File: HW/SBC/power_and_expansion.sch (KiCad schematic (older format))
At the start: 9 parts, among them J4 POWER IN, J5 Expansion Port, U11 LM7805CT

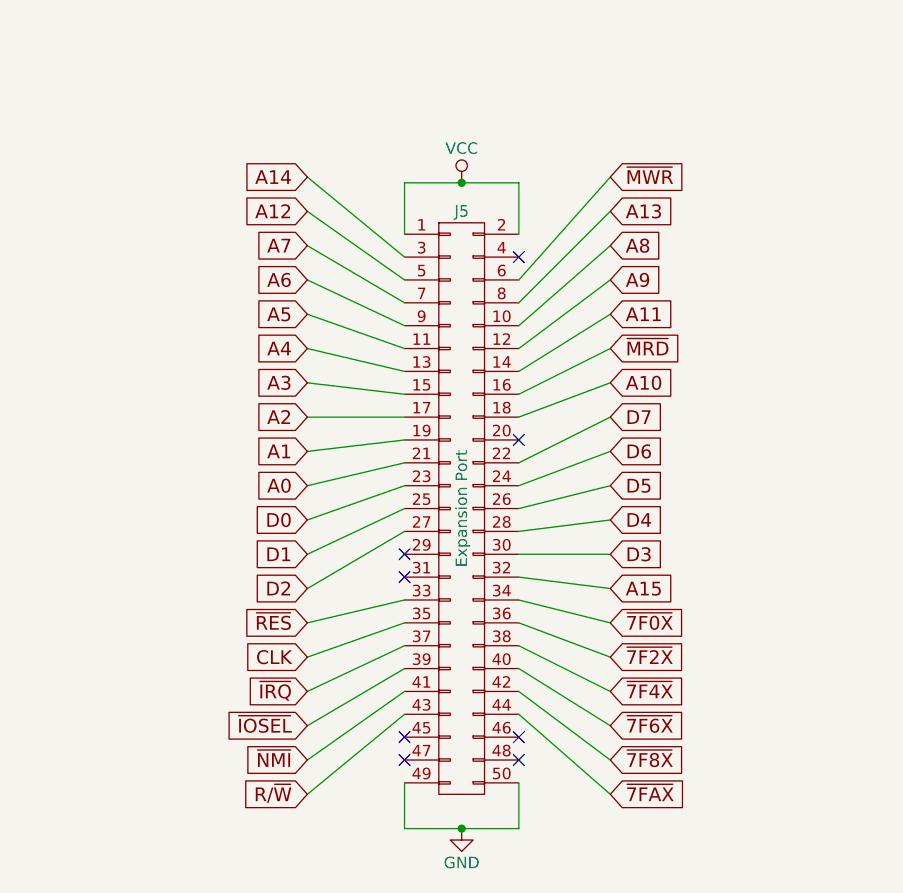
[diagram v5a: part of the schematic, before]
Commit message: New SBC PCB. Started to split pluto_kernel.asm into bios, monitor and miniassembler/disassembler. Various other updates.
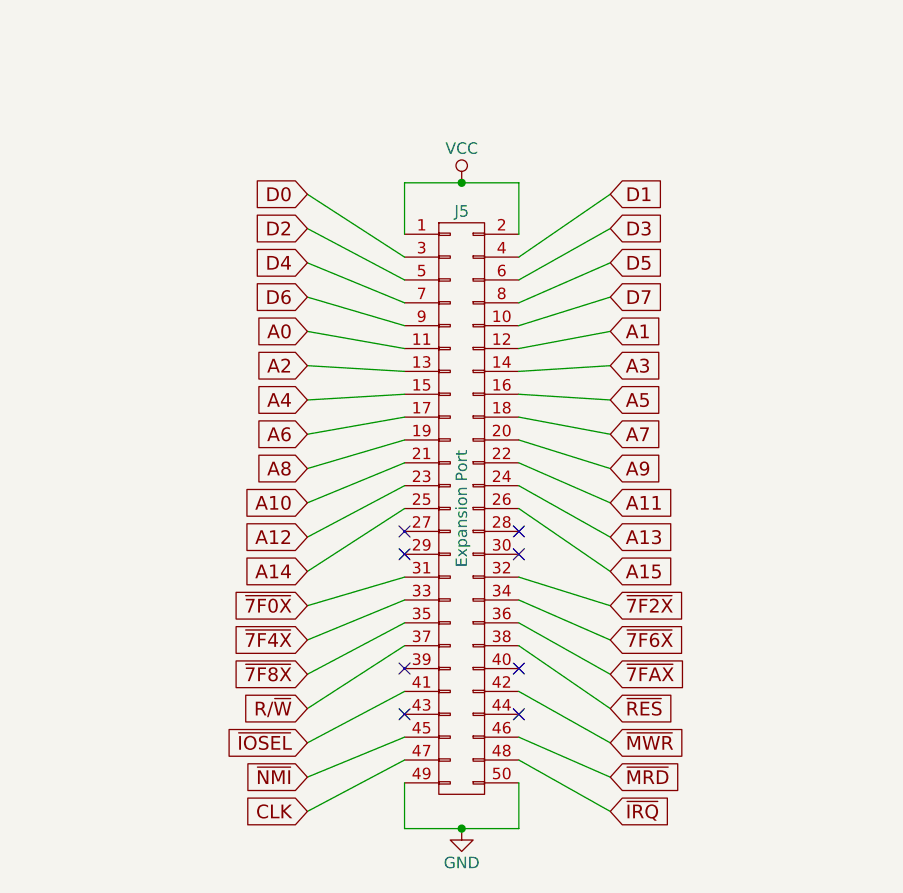
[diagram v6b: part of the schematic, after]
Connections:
- net A0: now also J5.11 (P11); no longer J5.21 (P21)
- net A1: now also J5.12 (P12); no longer J5.19 (P19)
- net A10: now also J5.21 (P21); no longer J5.18 (P18)
- net A11: now also J5.22 (P22); no longer J5.14 (P14)
- net A12: now also J5.23 (P23); no longer J5.5 (P5)
- net A13: now also J5.24 (P24); no longer J5.8 (P8)
- net A14: now also J5.25 (P25); no longer J5.3 (P3)
- net A15: now also J5.26 (P26); no longer J5.32 (P32)
- net A2: now also J5.13 (P13); no longer J5.17 (P17)
- net A3: now also J5.14 (P14); no longer J5.15 (P15)
- net A4: now also J5.15 (P15); no longer J5.13 (P13)
- net A5: now also J5.16 (P16); no longer J5.11 (P11)
- net A6: now also J5.17 (P17); no longer J5.9 (P9)
- net A7: now also J5.18 (P18); no longer J5.7 (P7)
- net A8: now also J5.19 (P19); no longer J5.10 (P10)
- net A9: now also J5.20 (P20); no longer J5.12 (P12)
- net CLK: now also J5.47 (P47); no longer J5.35 (P35)
- net D0: now also J5.3 (P3); no longer J5.23 (P23)
- net D1: now also J5.4 (P4); no longer J5.25 (P25)
- net D2: now also J5.5 (P5); no longer J5.27 (P27)
- net D3: now also J5.6 (P6); no longer J5.30 (P30)
- net D4: now also J5.7 (P7); no longer J5.28 (P28)
- net D5: now also J5.8 (P8); no longer J5.26 (P26)
- net D6: now also J5.9 (P9); no longer J5.24 (P24)
- net D7: now also J5.10 (P10); no longer J5.22 (P22)
- net R/~W: now also J5.37 (P37); no longer J5.43 (P43)
- net ~7F0X: now also J5.31 (P31); no longer J5.34 (P34)
- net ~7F2X: now also J5.32 (P32); no longer J5.36 (P36)
- net ~7F4X: now also J5.33 (P33); no longer J5.38 (P38)
- net ~7F6X: now also J5.34 (P34); no longer J5.40 (P40)
- net ~7F8X: now also J5.35 (P35); no longer J5.42 (P42)
- net ~7FAX: now also J5.36 (P36); no longer J5.44 (P44)
- net ~IOSEL: now also J5.41 (P41); no longer J5.39 (P39)
- net ~IRQ: now also J5.48 (P48); no longer J5.37 (P37)
- net ~MRD: now also J5.46 (P46); no longer J5.16 (P16)
- net ~MWR: now also J5.42 (P42); no longer J5.6 (P6)
- net ~NMI: now also J5.45 (P45); no longer J5.41 (P41)
- net ~RES: now also J5.38 (P38); no longer J5.33 (P33)
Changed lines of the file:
@@
 $EndComp
 $Comp
-L VCC #PWR025
+L VCC #PWR024
 U 1 1 58D5EE10
 P 5625 1650
-F 0 "#PWR025" H 5625 1500 50  0001 C CNN
+F 0 "#PWR024" H 5625 1500 50  0001 C CNN
 F 1 "VCC" H 5625 1800 50  0000 C CNN
 F 2 "" H 5625 1650 50  0001 C CNN
@@
 	3225 1650 5625 1650
 $Comp
-L VCC #PWR026
+L VCC #PWR025
 U 1 1 58D7686C
 P 3600 3500
-F 0 "#PWR026" H 3600 3350 50  0001 C CNN
+F 0 "#PWR025" H 3600 3350 50  0001 C CNN
 F 1 "VCC" H 3600 3650 50  0000 C CNN
 F 2 "" H 3600 3500 50  0001 C CNN
@@
 Connection ~ 3600 3500
 $Comp
-L GND #PWR027
+L GND #PWR026
 U 1 1 58D76B4A
 P 3600 6325
-F 0 "#PWR027" H 3600 6075 50  0001 C CNN
+F 0 "#PWR026" H 3600 6075 50  0001 C CNN
 F 1 "GND" H 3600 6175 50  0000 C CNN
 F 2 "" H 3600 6325 50  0001 C CNN
@@
 	3850 6325 3850 6125
 Connection ~ 3600 6325
-NoConn ~ 3850 3825
-Text GLabel 2925 4825 0    60   Input ~ 0
+Text GLabel 2925 4150 0    60   Input ~ 0
 A0
-Text GLabel 2925 4675 0    60   Input ~ 0
+Text GLabel 4250 4150 2    60   Input ~ 0
 A1
-Text GLabel 2925 4525 0    60   Input ~ 0
+Text GLabel 2925 4300 0    60   Input ~ 0
 A2
-Text GLabel 2925 4375 0    60   Input ~ 0
+Text GLabel 4250 4300 2    60   Input ~ 0
 A3
-Text GLabel 2925 4225 0    60   Input ~ 0
+Text GLabel 2925 4450 0    60   Input ~ 0
 A4
-Text GLabel 2925 4075 0    60   Input ~ 0
+Text GLabel 4250 4450 2    60   Input ~ 0
 A5
-Text GLabel 2925 3925 0    60   Input ~ 0
+Text GLabel 2925 4600 0    60   Input ~ 0
 A6
-Text GLabel 2925 3775 0    60   Input ~ 0
+Text GLabel 4250 4600 2    60   Input ~ 0
 A7
-Text GLabel 4250 3775 2    60   Input ~ 0
+Text GLabel 2925 4750 0    60   Input ~ 0
 A8
-Text GLabel 4250 3925 2    60   Input ~ 0
+Text GLabel 4250 4750 2    60   Input ~ 0
 A9
-Text GLabel 4250 4375 2    60   Input ~ 0
+Text GLabel 2925 4900 0    60   Input ~ 0
 A10
-Text GLabel 4250 4075 2    60   Input ~ 0
+Text GLabel 4250 4900 2    60   Input ~ 0
 A11
-Text GLabel 2925 3625 0    60   Input ~ 0
+Text GLabel 2925 5050 0    60   Input ~ 0
 A12
-Text GLabel 4250 3625 2    60   Input ~ 0
+Text GLabel 4250 5050 2    60   Input ~ 0
 A13
-Text GLabel 2925 3475 0    60   Input ~ 0
+Text GLabel 2925 5200 0    60   Input ~ 0
 A14
-Text GLabel 4250 5275 2    60   Input ~ 0
+Text GLabel 4250 5200 2    60   Input ~ 0
 A15
-Text GLabel 4250 3475 2    60   Input ~ 0
+Text GLabel 4250 5950 2    60   Input ~ 0
 ~MWR
-Text GLabel 4250 4225 2    60   Input ~ 0
+Text GLabel 4250 6100 2    60   Input ~ 0
 ~MRD
-Text GLabel 4250 5425 2    60   Input ~ 0
+Text GLabel 2925 5350 0    60   Input ~ 0
 ~7F0X
-Text GLabel 4250 5575 2    60   Input ~ 0
+Text GLabel 4250 5350 2    60   Input ~ 0
 ~7F2X
-Text GLabel 4250 5725 2    60   Input ~ 0
+Text GLabel 2925 5500 0    60   Input ~ 0
 ~7F4X
-Text GLabel 4250 5875 2    60   Input ~ 0
+Text GLabel 4250 5500 2    60   Input ~ 0
 ~7F6X
-Text GLabel 4250 6025 2    60   Input ~ 0
+Text GLabel 2925 5650 0    60   Input ~ 0
 ~7F8X
-Text GLabel 2925 4975 0    60   Input ~ 0
+Text GLabel 2925 3550 0    60   Input ~ 0
 D0
-Text GLabel 2925 5125 0    60   Input ~ 0
+Text GLabel 4250 3550 2    60   Input ~ 0
 D1
-Text GLabel 2925 5275 0    60   Input ~ 0
+Text GLabel 2925 3700 0    60   Input ~ 0
 D2
-Text GLabel 4250 5125 2    60   Input ~ 0
+Text GLabel 4250 3700 2    60   Input ~ 0
 D3
-Text GLabel 4250 4975 2    60   Input ~ 0
+Text GLabel 2925 3850 0    60   Input ~ 0
 D4
-Text GLabel 4250 4825 2    60   Input ~ 0
+Text GLabel 4250 3850 2    60   Input ~ 0
 D5
-Text GLabel 4250 4675 2    60   Input ~ 0
+Text GLabel 2925 4000 0    60   Input ~ 0
 D6
-Text GLabel 4250 4525 2    60   Input ~ 0
+Text GLabel 4250 4000 2    60   Input ~ 0
 D7
-Text GLabel 2925 5575 0    60   Input ~ 0
+Text GLabel 2925 6250 0    60   Input ~ 0
 CLK
-Text GLabel 2925 5725 0    60   Input ~ 0
+Text GLabel 4250 6250 2    60   Input ~ 0
 ~IRQ
-Text GLabel 2925 5875 0    60   Input ~ 0
+Text GLabel 2925 5950 0    60   Input ~ 0
 ~IOSEL
-Text GLabel 2925 6025 0    60   Input ~ 0
+Text GLabel 2925 6100 0    60   Input ~ 0
 ~NMI
-Text GLabel 2925 6175 0    60   Input ~ 0
+Text GLabel 2925 5800 0    60   Input ~ 0
 R/~W
-Text GLabel 2925 5425 0    60   Input ~ 0
+Text GLabel 4250 5800 2    60   Input ~ 0
 ~RES
-NoConn ~ 3350 5125
-NoConn ~ 3350 5225
-NoConn ~ 3850 4625
-NoConn ~ 3350 5925
-NoConn ~ 3350 6025
-Wire Wire Line
-	3350 3825 2925 3475
-Wire Wire Line
-	3350 3925 2925 3625
-Wire Wire Line
-	3350 4025 2925 3775
-Wire Wire Line
-	3350 4125 2925 3925
-Wire Wire Line
-	3350 4225 2925 4075
-Wire Wire Line
-	3350 4325 2925 4225
-Wire Wire Line
-	3350 4425 2925 4375
-Wire Wire Line
-	3350 4525 2925 4525
-Wire Wire Line
-	3350 4625 2925 4675
-Wire Wire Line
-	3350 4725 2925 4825
-Wire Wire Line
-	3350 4825 2925 4975
-Wire Wire Line
-	3350 4925 2925 5125
-Wire Wire Line
-	3350 5025 2925 5275
-Wire Wire Line
-	2925 5425 3350 5325
-Wire Wire Line
-	2925 5575 3350 5425
-Wire Wire Line
-	2925 5725 3350 5525
-Wire Wire Line
-	2925 5875 3350 5625
-Wire Wire Line
-	2925 6025 3350 5725
-Wire Wire Line
-	2925 6175 3350 5825
-Wire Wire Line
-	4250 3475 3850 3925
-Wire Wire Line
-	4250 3625 3850 4025
-Wire Wire Line
-	4250 3775 3850 4125
-Wire Wire Line
-	4250 3925 3850 4225
-Wire Wire Line
-	4250 4075 3850 4325
-Wire Wire Line
-	4250 4225 3850 4425
-Wire Wire Line
-	4250 4375 3850 4525
-Wire Wire Line
-	4250 4525 3850 4725
-Wire Wire Line
-	4250 4675 3850 4825
-Wire Wire Line
-	4250 4825 3850 4925
-Wire Wire Line
-	4250 4975 3850 5025
-Wire Wire Line
-	4250 5125 3850 5125
-Wire Wire Line
-	4250 5275 3850 5225
-Wire Wire Line
-	4250 5425 3850 5325
-Wire Wire Line
-	4250 5575 3850 5425
-Wire Wire Line
-	4250 5725 3850 5525
-Wire Wire Line
-	4250 5875 3850 5625
-Wire Wire Line
-	4250 6025 3850 5725
-NoConn ~ 3850 5925
-NoConn ~ 3850 6025
 Connection ~ 3225 2500
 $Comp
-L GND #PWR028
+L GND #PWR027
 U 1 1 58D85868
 P 5625 2500
-F 0 "#PWR028" H 5625 2250 50  0001 C CNN
+F 0 "#PWR027" H 5625 2250 50  0001 C CNN
 F 1 "GND" H 5625 2350 50  0000 C CNN
 F 2 "" H 5625 2500 50  0001 C CNN
@@
 	1    0    0    -1
 $EndComp
-Text GLabel 4250 6175 2    60   Input ~ 0
+Text GLabel 4250 5650 2    60   Input ~ 0
 ~7FAX
-Wire Wire Line
-	4250 6175 3850 5825
 $Comp
 L LM7805CT U11
@@
 	1    0    0    -1
 $EndComp
+Wire Wire Line
+	3350 3825 2925 3550
+Wire Wire Line
+	3350 3925 2925 3700
+Wire Wire Line
+	3350 4025 2925 3850
+Wire Wire Line
+	3350 4125 2925 4000
+Wire Wire Line
+	3350 4225 2925 4150
+Wire Wire Line
+	3350 4325 2925 4300
+Wire Wire Line
+	3350 4425 2925 4450
+Wire Wire Line
+	3350 4525 2925 4600
+Wire Wire Line
+	3350 4625 2925 4750
+Wire Wire Line
+	3350 4725 2925 4900
+Wire Wire Line
+	3350 4825 2925 5050
+Wire Wire Line
+	3350 4925 2925 5200
+Wire Wire Line
+	3850 3825 4250 3550
+Wire Wire Line
+	3850 3925 4250 3700
+Wire Wire Line
+	3850 4025 4250 3850
+Wire Wire Line
+	3850 4125 4250 4000
+Wire Wire Line
+	3850 4225 4250 4150
+Wire Wire Line
+	3850 4325 4250 4300
+Wire Wire Line
+	3850 4425 4250 4450
+Wire Wire Line
+	3850 4525 4250 4600
+Wire Wire Line
+	3850 4625 4250 4750
+Wire Wire Line
+	3850 4725 4250 4900
+Wire Wire Line
+	3850 4825 4250 5050
+Wire Wire Line
+	3850 4925 4250 5200
+Wire Wire Line
+	3350 5225 2925 5350
+Wire Wire Line
+	3350 5325 2925 5500
+Wire Wire Line
+	3350 5425 2925 5650
+Wire Wire Line
+	3350 5525 2925 5800
+Wire Wire Line
+	3350 5725 2925 5950
+Wire Wire Line
+	3350 5925 2925 6100
+Wire Wire Line
+	3350 6025 2925 6250
+Wire Wire Line
+	3850 5225 4250 5350
+Wire Wire Line
+	3850 5325 4250 5500
+Wire Wire Line
+	3850 5425 4250 5650
+Wire Wire Line
+	3850 5525 4250 5800
+Wire Wire Line
+	3850 5725 4250 5950
+Wire Wire Line
+	3850 5925 4250 6100
+Wire Wire Line
+	3850 6025 4250 6250
+NoConn ~ 3850 5025
+NoConn ~ 3850 5125
+NoConn ~ 3350 5025
+NoConn ~ 3350 5125
+NoConn ~ 3350 5625
+NoConn ~ 3850 5625
+NoConn ~ 3350 5825
+NoConn ~ 3850 5825
 $EndSCHEMATC

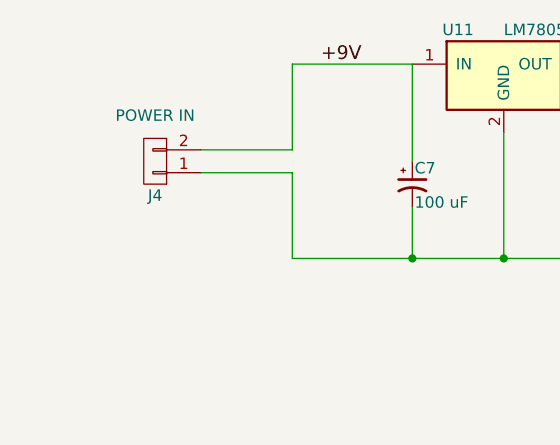
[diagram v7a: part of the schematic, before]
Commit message: New schema. Adding a VIA and sound chip.
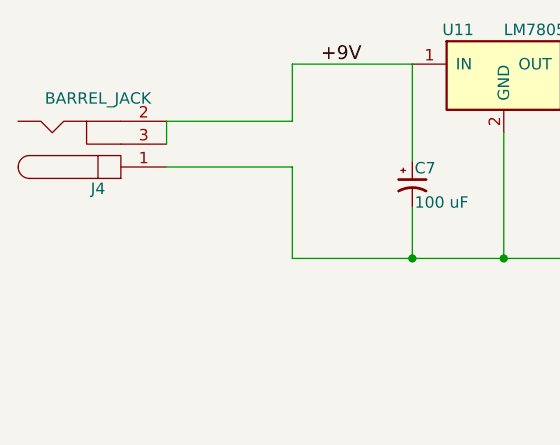
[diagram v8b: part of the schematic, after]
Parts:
- removed J4: POWER IN, Pin_Headers:Pin_Header_Straight_1x02_Pitch2.54mm, symbol CONN_01X02
- added J4: BARREL_JACK, Connect:BARREL_JACK, symbol BARREL_JACK
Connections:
- net +9V: now also J4.2, J4.3
- net GND: now also J4.1
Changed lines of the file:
@@
 LIBS:zetex
 LIBS:Zilog
+LIBS:pluto
 LIBS:pluto-cache
 EELAYER 25 0
@@
 $Descr A4 11693 8268
 encoding utf-8
-Sheet 6 6
+Sheet 6 7
 Title "Expansion port, power supply and decoupling capacitators"
 Date "2017-03-25"
@@
 $EndComp
 $Comp
-L VCC #PWR035
+L VCC #PWR42
 U 1 1 58D5EE10
 P 5625 1650
-F 0 "#PWR035" H 5625 1500 50  0001 C CNN
+F 0 "#PWR42" H 5625 1500 50  0001 C CNN
 F 1 "VCC" H 5625 1800 50  0000 C CNN
 F 2 "" H 5625 1650 50  0001 C CNN
@@
 	1    5625 1650
 	1    0    0    -1
-$EndComp
-$Comp
-L CONN_01X02 J4
-U 1 1 58D74BEC
-P 1300 2075
-F 0 "J4" H 1300 2225 50  0000 C CNN
-F 1 "POWER IN" H 1300 1875 50  0000 C CNN
-F 2 "Pin_Headers:Pin_Header_Straight_1x02_Pitch2.54mm" H 1300 2075 50  0001 C CNN
-F 3 "" H 1300 2075 50  0001 C CNN
-	1    1300 2075
-	-1   0    0    1
 $EndComp
 Text Label 2025 1650 0    60   ~ 0
@@
 	2425 1650 1900 1650
 Wire Wire Line
-	1500 2025 1900 2025
-Wire Wire Line
-	1900 2025 1900 1650
-Wire Wire Line
-	1500 2125 1900 2125
-Wire Wire Line
-	1900 2125 1900 2500
+	1350 1900 1900 1900
+Wire Wire Line
+	1900 1900 1900 1650
+Wire Wire Line
+	1350 2100 1900 2100
+Wire Wire Line
+	1900 2100 1900 2500
 Wire Wire Line
 	3225 1650 5625 1650
 $Comp
-L VCC #PWR036
+L VCC #PWR40
 U 1 1 58D7686C
 P 3600 3500
-F 0 "#PWR036" H 3600 3350 50  0001 C CNN
+F 0 "#PWR40" H 3600 3350 50  0001 C CNN
 F 1 "VCC" H 3600 3650 50  0000 C CNN
 F 2 "" H 3600 3500 50  0001 C CNN
@@
 Connection ~ 3600 3500
 $Comp
-L GND #PWR037
+L GND #PWR41
 U 1 1 58D76B4A
 P 3600 6325
-F 0 "#PWR037" H 3600 6075 50  0001 C CNN
+F 0 "#PWR41" H 3600 6075 50  0001 C CNN
 F 1 "GND" H 3600 6175 50  0000 C CNN
 F 2 "" H 3600 6325 50  0001 C CNN
@@
 Connection ~ 3225 2500
 $Comp
-L GND #PWR038
+L GND #PWR43
 U 1 1 58D85868
 P 5625 2500
-F 0 "#PWR038" H 5625 2250 50  0001 C CNN
+F 0 "#PWR43" H 5625 2250 50  0001 C CNN
 F 1 "GND" H 5625 2350 50  0000 C CNN
 F 2 "" H 5625 2500 50  0001 C CNN
@@
 NoConn ~ 3350 5825
 NoConn ~ 3850 5825
+$Comp
+L BARREL_JACK J4
+U 1 1 5930508B
+P 1050 2000
+F 0 "J4" H 1050 2195 50  0000 C CNN
+F 1 "BARREL_JACK" H 1050 1800 50  0000 C CNN
+F 2 "Connect:BARREL_JACK" H 1050 2000 50  0001 C CNN
+F 3 "" H 1050 2000 50  0001 C CNN
+	1    1050 2000
+	1    0    0    1
+$EndComp
+Wire Wire Line
+	1350 1900 1350 2000
 $EndSCHEMATC
